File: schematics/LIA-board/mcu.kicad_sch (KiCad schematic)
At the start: 1 part, among them U2 STM32U575RGTx

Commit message: modified scematic
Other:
- moved on the sheet: U2
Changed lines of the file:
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@@
 	(paper "A4")
 	(junction
-		(at 142.24 129.54)
+		(at 144.78 140.97)
 		(diameter 0)
 		(color 0 0 0 0)
@@
 	(wire
 		(pts
-			(xy 140.97 129.54) (xy 142.24 129.54)
-		)
-		(stroke
-			(width 0)
-			(type default)
-		)
-	)
-	(wire
-		(pts
-			(xy 142.24 129.54) (xy 142.24 130.81)
-		)
-		(stroke
-			(width 0)
-			(type default)
-		)
-	)
-	(wire
-		(pts
-			(xy 142.24 129.54) (xy 143.51 129.54)
-		)
-		(stroke
-			(width 0)
-			(type default)
-		)
-	)
-	(wire
-		(pts
-			(xy 140.97 127) (xy 140.97 129.54)
-		)
-		(stroke
-			(width 0)
-			(type default)
-		)
-	)
-	(wire
-		(pts
-			(xy 143.51 129.54) (xy 143.51 127)
+			(xy 143.51 140.97) (xy 144.78 140.97)
+		)
+		(stroke
+			(width 0)
+			(type default)
+		)
+	)
+	(wire
+		(pts
+			(xy 144.78 140.97) (xy 144.78 142.24)
+		)
+		(stroke
+			(width 0)
+			(type default)
+		)
+	)
+	(wire
+		(pts
+			(xy 144.78 140.97) (xy 146.05 140.97)
+		)
+		(stroke
+			(width 0)
+			(type default)
+		)
+	)
+	(wire
+		(pts
+			(xy 143.51 138.43) (xy 143.51 140.97)
+		)
+		(stroke
+			(width 0)
+			(type default)
+		)
+	)
+	(wire
+		(pts
+			(xy 146.05 140.97) (xy 146.05 138.43)
 		)
 		(stroke
@@
 	(symbol
 		(lib_id "MCU_ST_STM32U5:STM32U575RGTx")
-		(at 140.97 81.28 0)
+		(at 143.51 92.71 0)
 		(unit 1)
 		(body_style 1)
@@
 		(fields_autoplaced yes)
 		(property "Reference" "U2"
-			(at 145.6533 127 0)
+			(at 148.1933 138.43 0)
 			(show_name no)
 			(do_not_autoplace no)
@@
 		)
 		(property "Value" "STM32U575RGTx"
-			(at 145.6533 129.54 0)
+			(at 148.1933 140.97 0)
 			(show_name no)
 			(do_not_autoplace no)
@@
 		)
 		(property "Footprint" "Package_QFP:LQFP-64_10x10mm_P0.5mm"
-			(at 125.73 124.46 0)
+			(at 128.27 135.89 0)
 			(hide yes)
 			(show_name no)
@@
 		)
 		(property "Datasheet" "https://www.st.com/resource/en/datasheet/stm32u575rg.pdf"
-			(at 140.97 81.28 0)
+			(at 143.51 92.71 0)
 			(hide yes)
 			(show_name no)
@@
 		)
 		(property "Description" "STMicroelectronics Arm Cortex-M33 MCU, 1024KB flash, 786KB RAM, 160 MHz, 1.71-3.6V, 51 GPIO, LQFP64"
-			(at 140.97 81.28 0)
+			(at 143.51 92.71 0)
 			(hide yes)
 			(show_name no)
@@
 	(symbol
 		(lib_id "power:GND")
-		(at 142.24 130.81 0)
+		(at 144.78 142.24 0)
 		(unit 1)
 		(body_style 1)
@@
 		(fields_autoplaced yes)
 		(property "Reference" "#PWR070"
-			(at 142.24 137.16 0)
+			(at 144.78 148.59 0)
 			(hide yes)
 			(show_name no)
@@
 		)
 		(property "Value" "GND"
-			(at 142.24 135.89 0)
+			(at 144.78 147.32 0)
 			(show_name no)
 			(do_not_autoplace no)
@@
 		)
 		(property "Footprint" ""
-			(at 142.24 130.81 0)
+			(at 144.78 142.24 0)
 			(hide yes)
 			(show_name no)
@@
 		)
 		(property "Datasheet" ""
-			(at 142.24 130.81 0)
+			(at 144.78 142.24 0)
 			(hide yes)
 			(show_name no)
@@
 		)
 		(property "Description" "Power symbol creates a global label with name \"GND\" , ground"
-			(at 142.24 130.81 0)
-			(hide yes)
-			(show_name no)
+			(at 144.78 142.24 0)
+			(hide yes)
+			(show_name no)

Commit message: some changes to board
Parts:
- added U19: CP2102N-Axx-xQFN20, Package_DFN_QFN:SiliconLabs_QFN-20-1EP_3x3mm_P0.5mm, symbol Interface_USB:CP2102N-Axx-xQFN20
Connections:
- new net: U19.12 (GND), U19.21 (GND), U19.3 (GND)
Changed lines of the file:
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@@
+	)
+	(symbol
+		(lib_id "Interface_USB:CP2102N-Axx-xQFN20")
+		(at 60.96 99.06 0)
+		(unit 1)
+		(body_style 1)
+		(exclude_from_sim no)
+		(in_bom yes)
+		(on_board yes)
+		(in_pos_files yes)
+		(dnp no)
+		(fields_autoplaced yes)
+		(property "Reference" "U19"
+			(at 63.1033 127 0)
+			(show_name no)
+			(do_not_autoplace no)
+			(effects
+				(font
+					(size 1.27 1.27)
+				)
+				(justify left)
+			)
+		)
+		(property "Value" "CP2102N-Axx-xQFN20"
+			(at 63.1033 129.54 0)
+			(show_name no)
+			(do_not_autoplace no)
+			(effects
+				(font
+					(size 1.27 1.27)
+				)
+				(justify left)
+			)
+		)
+		(property "Footprint" "Package_DFN_QFN:SiliconLabs_QFN-20-1EP_3x3mm_P0.5mm"
+			(at 92.71 125.73 0)
+			(hide yes)
+			(show_name no)
+			(do_not_autoplace no)
+			(effects
+				(font
+					(size 1.27 1.27)
+				)
+			)
+		)
+		(property "Datasheet" "https://www.silabs.com/documents/public/data-sheets/cp2102n-datasheet.pdf"
+			(at 62.23 118.11 0)
+			(hide yes)
+			(show_name no)
+			(do_not_autoplace no)
+			(effects
+				(font
+					(size 1.27 1.27)
+				)
+			)
+		)
+		(property "Description" "USB to UART master bridge, QFN-20"
+			(at 60.96 99.06 0)
+			(hide yes)
+			(show_name no)
+			(do_not_autoplace no)
+			(effects
+				(font
+					(size 1.27 1.27)
+				)
+			)
+		)
+		(pin "12"
+		)
+		(pin "13"
+		)
+		(pin "20"
+		)
+		(pin "3"
+		)
+		(pin "2"
+		)
+		(pin "4"
+		)
+		(pin "6"
+		)
+		(pin "10"
+		)
+		(pin "15"
+		)
+		(pin "14"
+		)
+		(pin "5"
+		)
+		(pin "7"
+		)
+		(pin "16"
+		)
+		(pin "17"
+		)
+		(pin "1"
+		)
+		(pin "21"
+		)
+		(pin "9"
+		)
+		(pin "11"
+		)
+		(pin "8"
+		)
+		(pin "18"
+		)
+		(pin "19"
+		)
+		(instances
+			(project "GMOS-LIA"
+				(path "/87b3d1ed-39bd-4cff-a405-e580c48ff0ef/1c6f142e-1df0-4fd8-8558-8d862b0034c2"
+					(reference "U19")
+					(unit 1)
+				)
+			)
+		)
 	)
 	(symbol

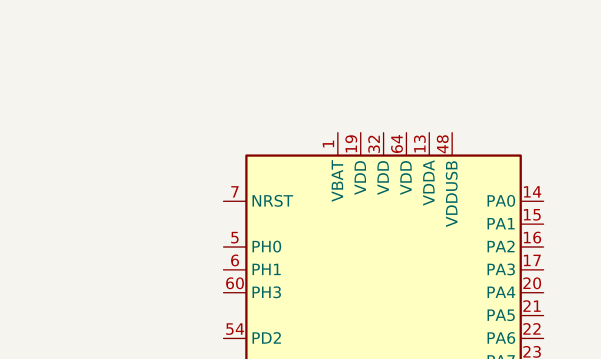
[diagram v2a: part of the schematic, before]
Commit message: commit before changing the oscillator implementation
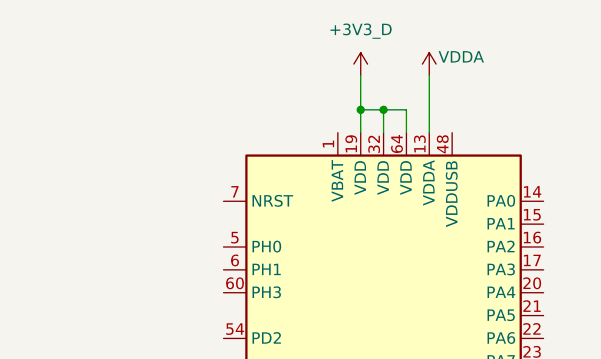
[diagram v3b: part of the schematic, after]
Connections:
- net VDDA: now reaches U2.13 (VDDA)
- net +3V3_D: now reaches U2.19 (VDD)
- net +3V3_D: now also U2.32 (VDD), U2.64 (VDD)
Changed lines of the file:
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@@
 	(paper "A4")
+	(junction
+		(at 143.51 41.91)
+		(diameter 0)
+		(color 0 0 0 0)
+	)
 	(junction
 		(at 144.78 140.97)
@@
 		(color 0 0 0 0)
 	)
+	(junction
+		(at 140.97 41.91)
+		(diameter 0)
+		(color 0 0 0 0)
+	)
+	(wire
+		(pts
+			(xy 140.97 38.1) (xy 140.97 41.91)
+		)
+		(stroke
+			(width 0)
+			(type default)
+		)
+	)
+	(wire
+		(pts
+			(xy 140.97 44.45) (xy 140.97 41.91)
+		)
+		(stroke
+			(width 0)
+			(type default)
+		)
+	)
+	(wire
+		(pts
+			(xy 148.59 38.1) (xy 148.59 44.45)
+		)
+		(stroke
+			(width 0)
+			(type default)
+		)
+	)
 	(wire
 		(pts
@@
 	(wire
 		(pts
+			(xy 143.51 41.91) (xy 143.51 44.45)
+		)
+		(stroke
+			(width 0)
+			(type default)
+		)
+	)
+	(wire
+		(pts
 			(xy 144.78 140.97) (xy 146.05 140.97)
+		)
+		(stroke
+			(width 0)
+			(type default)
+		)
+	)
+	(wire
+		(pts
+			(xy 146.05 41.91) (xy 146.05 44.45)
+		)
+		(stroke
+			(width 0)
+			(type default)
+		)
+	)
+	(wire
+		(pts
+			(xy 143.51 41.91) (xy 146.05 41.91)
+		)
+		(stroke
+			(width 0)
+			(type default)
+		)
+	)
+	(wire
+		(pts
+			(xy 140.97 41.91) (xy 143.51 41.91)
 		)
 		(stroke
@@
 					(unit 1)
 				)
+			)
+		)
+	)
+	(symbol
+		(lib_id "power:VDDA")
+		(at 148.59 38.1 0)
+		(unit 1)
+		(body_style 1)
+		(exclude_from_sim no)
+		(in_bom yes)
+		(on_board yes)
+		(in_pos_files yes)
+		(dnp no)
+		(property "Reference" "#PWR0119"
+			(at 148.59 41.91 0)
+			(hide yes)
+			(show_name no)
+			(do_not_autoplace no)
+			(effects
+				(font
+					(size 1.27 1.27)
+				)
+			)
+		)
+		(property "Value" "VDDA"
+			(at 152.146 36.068 0)
+			(show_name no)
+			(do_not_autoplace no)
+			(effects
+				(font
+					(size 1.27 1.27)
+				)
+			)
+		)
+		(property "Footprint" ""
+			(at 148.59 38.1 0)
+			(hide yes)
+			(show_name no)
+			(do_not_autoplace no)
+			(effects
+				(font
+					(size 1.27 1.27)
+				)
+			)
+		)
+		(property "Datasheet" ""
+			(at 148.59 38.1 0)
+			(hide yes)
+			(show_name no)
+			(do_not_autoplace no)
+			(effects
+				(font
+					(size 1.27 1.27)
+				)
+			)
+		)
+		(property "Description" "Power symbol creates a global label with name \"VDDA\""
+			(at 148.59 38.1 0)
+			(hide yes)
+			(show_name no)
+			(do_not_autoplace no)
+			(effects
+				(font
+					(size 1.27 1.27)
+				)
+			)
+		)
+		(pin "1"
+		)
+		(instances
+			(project "GMOS-LIA"
+				(path "/87b3d1ed-39bd-4cff-a405-e580c48ff0ef/1c6f142e-1df0-4fd8-8558-8d862b0034c2"
+					(reference "#PWR0119")
+					(unit 1)
+				)
+			)
+		)
+	)
+	(symbol
+		(lib_id "power:+3V3")
+		(at 140.97 38.1 0)
+		(unit 1)
+		(body_style 1)
+		(exclude_from_sim no)
+		(in_bom yes)
+		(on_board yes)
+		(in_pos_files yes)
+		(dnp no)
+		(fields_autoplaced yes)
+		(property "Reference" "#PWR0120"
+			(at 140.97 41.91 0)
+			(hide yes)
+			(show_name no)
+			(do_not_autoplace no)
+			(effects
+				(font
+					(size 1.27 1.27)
+				)
+			)
+		)
+		(property "Value" "+3V3_D"
+			(at 140.97 33.02 0)
+			(show_name no)
+			(do_not_autoplace no)
+			(effects
+				(font
+					(size 1.27 1.27)
+				)
+			)
+		)
+		(property "Footprint" ""
+			(at 140.97 38.1 0)
+			(hide yes)
+			(show_name no)
+			(do_not_autoplace no)
+			(effects
+				(font
+					(size 1.27 1.27)
+				)
+			)
+		)
+		(property "Datasheet" ""
+			(at 140.97 38.1 0)
+			(hide yes)
+			(show_name no)
+			(do_not_autoplace no)
+			(effects
+				(font
+					(size 1.27 1.27)
+				)
+			)
+		)
+		(property "Description" "Power symbol creates a global label with name \"+3V3\""
+			(at 140.97 38.1 0)
+			(hide yes)
+			(show_name no)
+			(do_not_autoplace no)
+			(effects
+				(font
+					(size 1.27 1.27)
+				)
+			)
+		)
+		(pin "1"
+		)
+		(instances
+			(project "GMOS-LIA"
+				(path "/87b3d1ed-39bd-4cff-a405-e580c48ff0ef/1c6f142e-1df0-4fd8-8558-8d862b0034c2"
+					(reference "#PWR0120")
+					(unit 1)
+				)

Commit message: commit before changing LIA
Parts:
- removed U19: CP2102N-Axx-xQFN20, Package_DFN_QFN:SiliconLabs_QFN-20-1EP_3x3mm_P0.5mm, symbol Interface_USB:CP2102N-Axx-xQFN20
- added C49: C, symbol Device:C
- added R40, R41: 33, SparkFun-Resistor:R_0603_1608Metric, symbol SparkFun:R
- added U11: ISO6721BD, Package_SO:SOIC-8_3.9x4.9mm_P1.27mm, symbol Isolator:ISO6721BD
- renumbered U2 to U12
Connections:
- net +3V3_D: now also U11.8 (VCC2)
- net GND: now also C49.1, U11.5 (GND2)
- net spi_sck: now reaches U12.15 (PA1)
- net mcu_uart_rx: now reaches U12.16 (PA2)
- net mcu_uart_rx: now also U11.7 (INA)
- net mcu_uart_tx: now reaches U12.17 (PA3)
- net mcu_uart_tx: now also U11.6 (OUTB)
- net mcu_sin_ref: now reaches U12.20 (PA4)
- net spi_miso: now reaches U12.22 (PA6)
- net spi_mosi: now reaches U12.23 (PA7)
- net at U12.46 (PA13): now also R40.1
- net at U12.49 (PA14): now also R41.1
- net osc_in: now reaches U12.5 (PH0)
- net mcu_i2c_scl: now reaches U12.58 (PB6)
- net mcu_i2c_sda: now reaches U12.59 (PB7)
- net msu_rst: now reaches U12.7 (NRST)
- net msu_rst: now also C49.2
- net V_imeas0: now reaches U12.8 (PC0)
- net V_imeas1: now reaches U12.9 (PC1)
- new net iso_gnd: U11.4 (GND1)
- new net iso_vcc: U11.1 (VCC1)
- new net swclk: R41.2
- new net swdio: R40.2
- new net uart_rx_iso: U11.2 (OUTA)
- new net uart_tx_iso: U11.3 (INB)

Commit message: major re-organization of documentation
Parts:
- added C52, C53, C54: C, symbol Device:C
- added Y1: 16MHz, Oscillator:Oscillator_SMD_SeikoEpson_SG210-4Pin_2.5x2.0mm, symbol Oscillator:SG-210STF
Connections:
- net +3V3_D: now also C52.2, C53.2, Y1.1 (~{ST}), Y1.4 (Vcc)
- net GND: now also C52.1, C53.1, C54.1, Y1.2 (GND)
- net osc_in: now also Y1.3 (OUT)
- net at U12.30 (VCAP): now also C54.2
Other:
- moved on the sheet: C49, R40, R41, U12
